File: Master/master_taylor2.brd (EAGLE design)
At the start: 54.1 x 51.3 mm, 47 parts, among them J1 ISP, K1 653002114822, K2 653002114822, K3 653002114822, K4 653002114822, U1 ATMEGA128RFA1, U2 TPS73633-DBVT, U3 ULN2003ADR, Y1 16MHz

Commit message: Added all-seeing eye to ward off evil electrons
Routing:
- net N$5: track 0.00 -> 19.3 mm
- net VBAT: track 252.8 -> 253.4 mm
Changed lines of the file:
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@@
 <setting verticaltext="up"/>
 </settings>
-<grid distance="0.5" unitdist="mm" unit="mm" style="lines" multiple="1" display="yes" altdistance="0.001" altunitdist="mm" altunit="mm"/>
+<grid distance="1" unitdist="mm" unit="mm" style="lines" multiple="1" display="yes" altdistance="0.001" altunitdist="mm" altunit="mm"/>
 <layers>
 <layer number="1" name="Top" color="4" fill="1" visible="yes" active="yes"/>
@@
 <plain>
 <rectangle x1="-27.289" y1="9.745" x2="-20.76" y2="12.254" layer="41"/>
+<wire x1="-20" y1="24" x2="-24" y2="17" width="0.3" layer="21"/>
+<wire x1="-24" y1="17" x2="-16" y2="17" width="0.3" layer="21"/>
+<wire x1="-16" y1="17" x2="-20" y2="24" width="0.3" layer="21"/>
+<wire x1="-18.069" y1="20.369" x2="-22.017" y2="20.341" width="0.3" layer="21" curve="-100"/>
+<wire x1="-22.039" y1="20.375" x2="-18.011" y2="20.498" width="0.3" layer="21" curve="-100"/>
+<circle x="-20.033" y="20.365" radius="0.757853125" width="0.3" layer="21"/>
 </plain>
 <attributes>
@@
 </element>
 <element name="C9" library="SparkFun-Capacitors" package="0603-CAP" value="0.75pF" x="-19" y="8" rot="R90"/>
-<element name="D1" library="led" package="CHIPLED_0603" value="RED" x="21.5" y="-11" rot="R180"/>
-<element name="D2" library="led" package="CHIPLED_0603" value="RED" x="19" y="-11" rot="R180"/>
-<element name="D3" library="led" package="CHIPLED_0603" value="GREEN" x="16.5" y="-11" rot="R180"/>
+<element name="D1" library="led" package="CHIPLED_0603" value="RED" x="21.5" y="-11" smashed="yes" rot="R180">
+<attribute name="NAME" x="22.146" y="-10.096" size="0.6096" layer="25" rot="R270"/>
+<attribute name="VALUE" x="20.379" y="-10.326" size="0.6096" layer="27" rot="R270"/>
+</element>
+<element name="D2" library="led" package="CHIPLED_0603" value="RED" x="19" y="-11" smashed="yes" rot="R180">
+<attribute name="NAME" x="17.879" y="-10.723" size="0.6096" layer="25" rot="R270"/>
+<attribute name="VALUE" x="17.468" y="-12.817" size="0.6096" layer="27"/>
+</element>
+<element name="D3" library="led" package="CHIPLED_0603" value="GREEN" x="16.5" y="-11" smashed="yes" rot="R180">
+<attribute name="NAME" x="15.327" y="-10.493" size="0.6096" layer="25" rot="R270"/>
+<attribute name="VALUE" x="14.48" y="-9.688" size="0.6096" layer="27" rot="R270"/>
+</element>
 <element name="J1" library="SparkFun-Connectors" package="2X3-NS" value="ISP" x="20.5" y="20.5" rot="R270"/>
 <element name="JP1" library="SparkFun-Connectors" package="1X04" value="Debugger" x="2" y="-22.5" rot="R180"/>
@@
 <wire x1="-19.875" y1="-17" x2="-19.96" y2="-16.905" width="0.254" layer="1"/>
 <wire x1="-9" y1="9.25" x2="-8" y2="9.25" width="0.254" layer="1"/>
-<wire x1="-21.25" y1="-3" x2="-9" y2="9.25" width="0.254" layer="1"/>
-<wire x1="-21.25" y1="-16.75" x2="-21.25" y2="-3" width="0.254" layer="1"/>
-<wire x1="-20" y1="-16.75" x2="-21.25" y2="-16.75" width="0.254" layer="1"/>
 <wire x1="-20" y1="-16.75" x2="-19.96" y2="-16.905" width="0.254" layer="1"/>
 <wire x1="17.25" y1="19.75" x2="19" y2="18" width="0.254" layer="1"/>
@@
 <via x="3.5" y="19.75" extent="1-16" drill="0.381"/>
 <via x="-9.5" y="9.75" extent="1-16" drill="0.381"/>
+<wire x1="-13.52" y1="-4.528" x2="-22" y2="-13.008" width="0.3" layer="1"/>
+<wire x1="-22" y1="-13.008" x2="-22" y2="-15" width="0.3" layer="1"/>
+<wire x1="-22" y1="-15" x2="-20.095" y2="-16.905" width="0.3" layer="1"/>
+<wire x1="-20.095" y1="-16.905" x2="-19.96" y2="-16.905" width="0.3" layer="1"/>
+<wire x1="-13.52" y1="-4.528" x2="-13.52" y2="-2.51" width="0.3" layer="1"/>
+<wire x1="-13.52" y1="-2.51" x2="-9.704" y2="1.306" width="0.3" layer="1"/>
+<wire x1="-9.704" y1="1.306" x2="-9.704" y2="9.546" width="0.3" layer="1"/>
+<wire x1="-9.704" y1="9.546" x2="-9.5" y2="9.75" width="0.3" layer="1"/>
 </signal>
 <signal name="PE4">
@@
 <wire x1="17.5" y1="-28.5" x2="-28" y2="-28.5" width="0.6096" layer="16"/>
 <wire x1="18" y1="-28" x2="17.5" y2="-28.5" width="0.6096" layer="16"/>
-<wire x1="19.5" y1="-26.5" x2="18" y2="-28" width="0.6096" layer="1"/>
-<wire x1="19.5" y1="-23" x2="19.5" y2="-26.5" width="0.6096" layer="1"/>
-<wire x1="20.5" y1="-22" x2="19.5" y2="-23" width="0.6096" layer="1"/>
-<wire x1="20.5" y1="-20" x2="20.5" y2="-22" width="0.6096" layer="1"/>
+<wire x1="20.5" y1="-25.5" x2="18" y2="-28" width="0.6096" layer="1"/>
+<wire x1="20.5" y1="-20" x2="20.5" y2="-25.5" width="0.6096" layer="1"/>
 <wire x1="21" y1="-19.5" x2="20.5" y2="-20" width="0.6096" layer="1"/>
 <wire x1="22.5" y1="-19.5" x2="21" y2="-19.5" width="0.6096" layer="1"/>
@@
 <via x="27" y="28.5" extent="1-16" drill="0.6"/>
 <via x="30" y="28.5" extent="1-16" drill="0.6"/>
-<wire x1="22" y1="-28.5" x2="27.5" y2="-28.5" width="0.6096" layer="1"/>
-<wire x1="20.5" y1="-27" x2="22" y2="-28.5" width="0.6096" layer="1"/>
-<wire x1="17.5" y1="-27" x2="20.5" y2="-27" width="0.6096" layer="16"/>
+<wire x1="21.5" y1="-28.5" x2="27.5" y2="-28.5" width="0.6096" layer="1"/>
 <wire x1="17" y1="-27.5" x2="17.5" y2="-27" width="0.6096" layer="16"/>
 <wire x1="-29.5" y1="-27.5" x2="17" y2="-27.5" width="0.6096" layer="16"/>
@@
 <wire x1="-35.5" y1="-36" x2="-35.417940625" y2="-36.061940625" width="0.6096" layer="1"/>
 <wire x1="28" y1="-28" x2="27.5" y2="-28.5" width="0.6096" layer="1"/>
-<via x="20.5" y="-27" extent="1-16" drill="0.6"/>
+<via x="21.5" y="-28.5" extent="1-16" drill="0.6"/>
 <via x="-29.5" y="-27.5" extent="1-16" drill="0.6"/>
 <wire x1="12.8016" y1="7.62" x2="13.1064" y2="7.62" width="0.254" layer="1"/>
@@
 <wire x1="13.3096" y1="9.4488" x2="13.2" y2="9.45" width="0.254" layer="1"/>
 <wire x1="22.2504" y1="7.112" x2="22.65" y2="7" width="0.254" layer="1"/>
+<wire x1="17.5" y1="-27" x2="21" y2="-27" width="0.6096" layer="16"/>
+<wire x1="21" y1="-28" x2="21" y2="-27" width="0.6096" layer="16"/>
+<wire x1="21.5" y1="-28.5" x2="21" y2="-28" width="0.6096" layer="16"/>
 </signal>
 <signal name="N$20">
@@
 <wire x1="27.5" y1="-12" x2="27.5" y2="-11.9" width="0.6096" layer="1"/>
 </signal>
+<signal name="N$5">
+<wire x1="-15" y1="24" x2="-17" y2="22" width="0.3" layer="1"/>
+<wire x1="-17" y1="22" x2="-15" y2="20" width="0.3" layer="1"/>
+<wire x1="-15" y1="20" x2="-13" y2="22" width="0.3" layer="1"/>
+<wire x1="-13" y1="22" x2="-15" y2="24" width="0.3" layer="1"/>
+<wire x1="-15" y1="24" x2="-15" y2="20" width="0.3" layer="1"/>
+<wire x1="-13" y1="22" x2="-17" y2="22" width="0.3" layer="1"/>
+</signal>
 </signals>

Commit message: ng
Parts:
- removed K1, K2, K3, K4: 653002114822, Wuerth_Elektronik_eiCan_Wire_to_Board_Connectors:653002114822
- added WING_BL, WING_BR, WING_FL, WING_FR: 653002114822, Wuerth_Elektronik_eiCan_Wire_to_Board_Connectors:653002114822
- moved R1 4.12 mm to (-15.0, -20.0)
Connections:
- net N$29: now also WING_BL.2; no longer K1.2
- net N$30: now also WING_BR.2; no longer K2.2
- net N$31: now also WING_FL.2; no longer K3.2
- net N$32: now also WING_FR.2; no longer K4.2
- net VBAT: now also WING_BL.1, WING_BR.1, WING_FL.1, WING_FR.1; no longer K1.1, K2.1, K3.1, K4.1
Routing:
- net N$5: track 19.3 -> 0.00 mm
- net 3.3V: track 179.1 -> 174.7 mm
- net VBAT: track 253.4 -> 255.9 mm
- net N$29: track 70.2 -> 71.6 mm
- net RESET: track 77.8 -> 79.0 mm
- net N$30: track 26.9 -> 27.6 mm
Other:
- board text added: "Changes: -Reduced area to save weight -Keepout underneath IMU based on official recommendation -Most parts are 0603 for compactness -Better placement on crystal and antenna -Wings are made for 7mm motors -Removed useless parts -Moved connectors to match wire length"

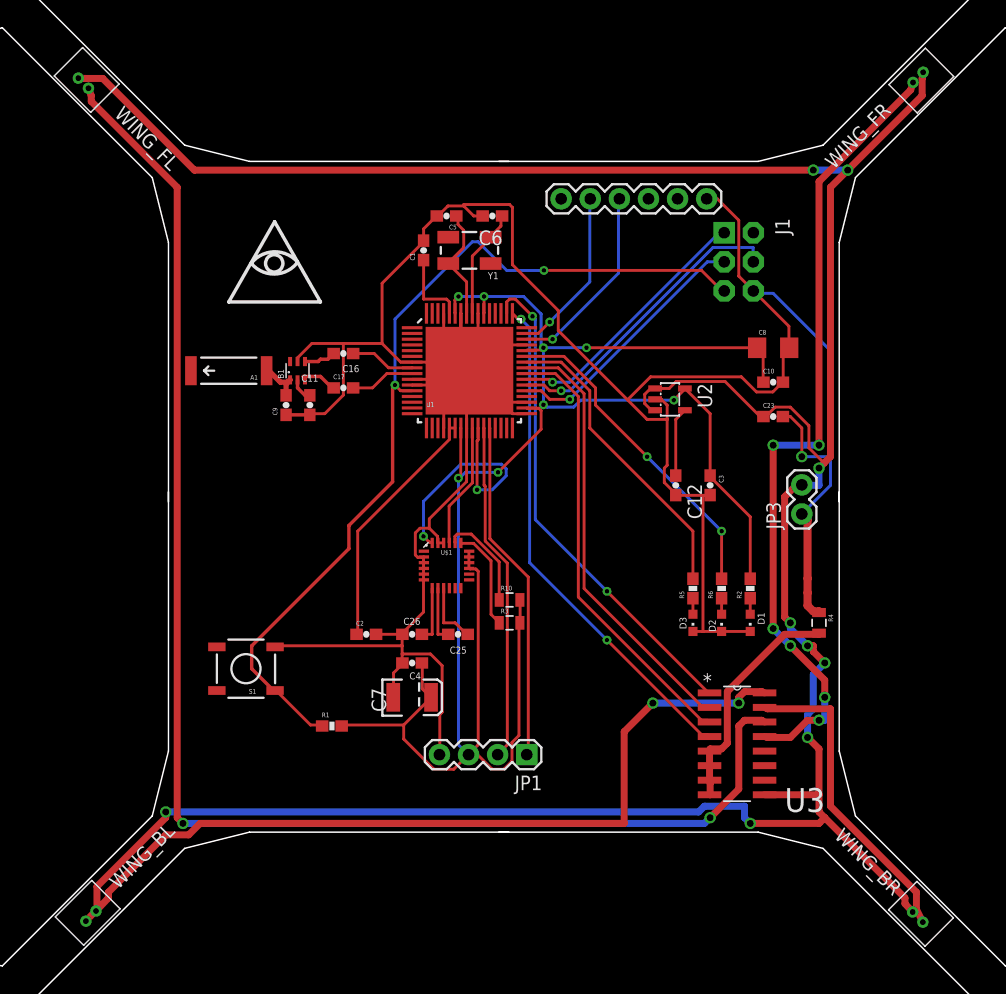
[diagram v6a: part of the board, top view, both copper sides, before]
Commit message: Added caps near each motor
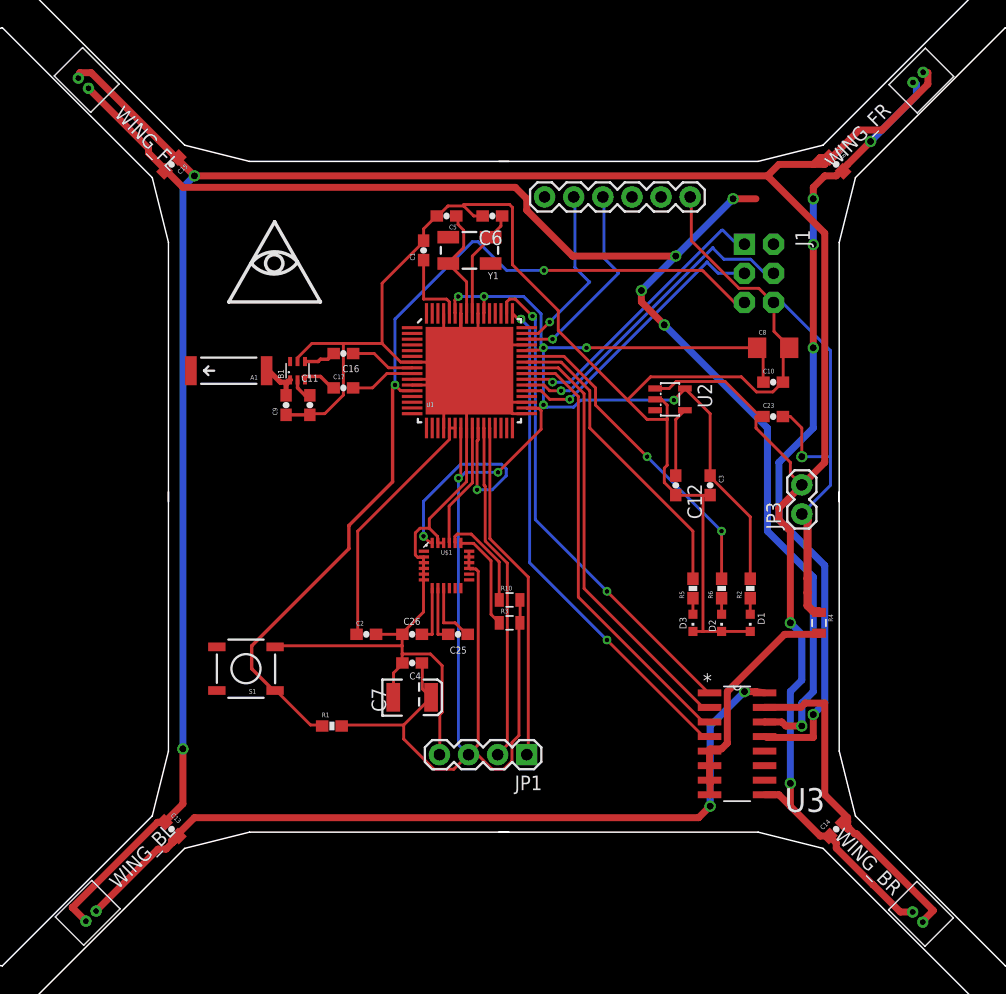
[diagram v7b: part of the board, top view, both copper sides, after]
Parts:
- added C13, C14, C15, C18: 10uF, SparkFun-Capacitors:0603-CAP
- moved J1 2.03 mm to (22.3, 19.5)
- moved JP9 1.45 mm to (3.56, 26.2)
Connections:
- removed net DTR: JP9.DTR
- net N$29: now also C13.2
- net N$30: now also C14.2
- net N$31: now also C15.2
- net N$32: now also C18.2
- net VBAT: now also C13.1, C14.1, C15.1, C18.1
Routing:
- net N$31: track 125.2 -> 119.7 mm, vias 2 -> 5
- net VBAT: track 255.9 -> 252.3 mm, vias 9 -> 4
- net N$30: track 27.6 -> 29.8 mm
- net SCK: track 22.5 -> 24.7 mm
- net MISO: track 22.9 -> 25.1 mm
- net RESET: track 79.0 -> 81.2 mm
- net MOSI: track 26.4 -> 27.9 mm
- net N$32: track 70.7 -> 69.4 mm, vias 6 -> 5
- net GND: track 276.0 -> 275.3 mm
- net TX0: track 14.7 -> 15.4 mm
- net RX0: track 17.0 -> 17.6 mm
